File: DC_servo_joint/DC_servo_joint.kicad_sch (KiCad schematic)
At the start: 49 parts, among them U1 AS5600, U2 ESP32-C3-WROOM-02, U3 SP3485EN, U5 TPS563200

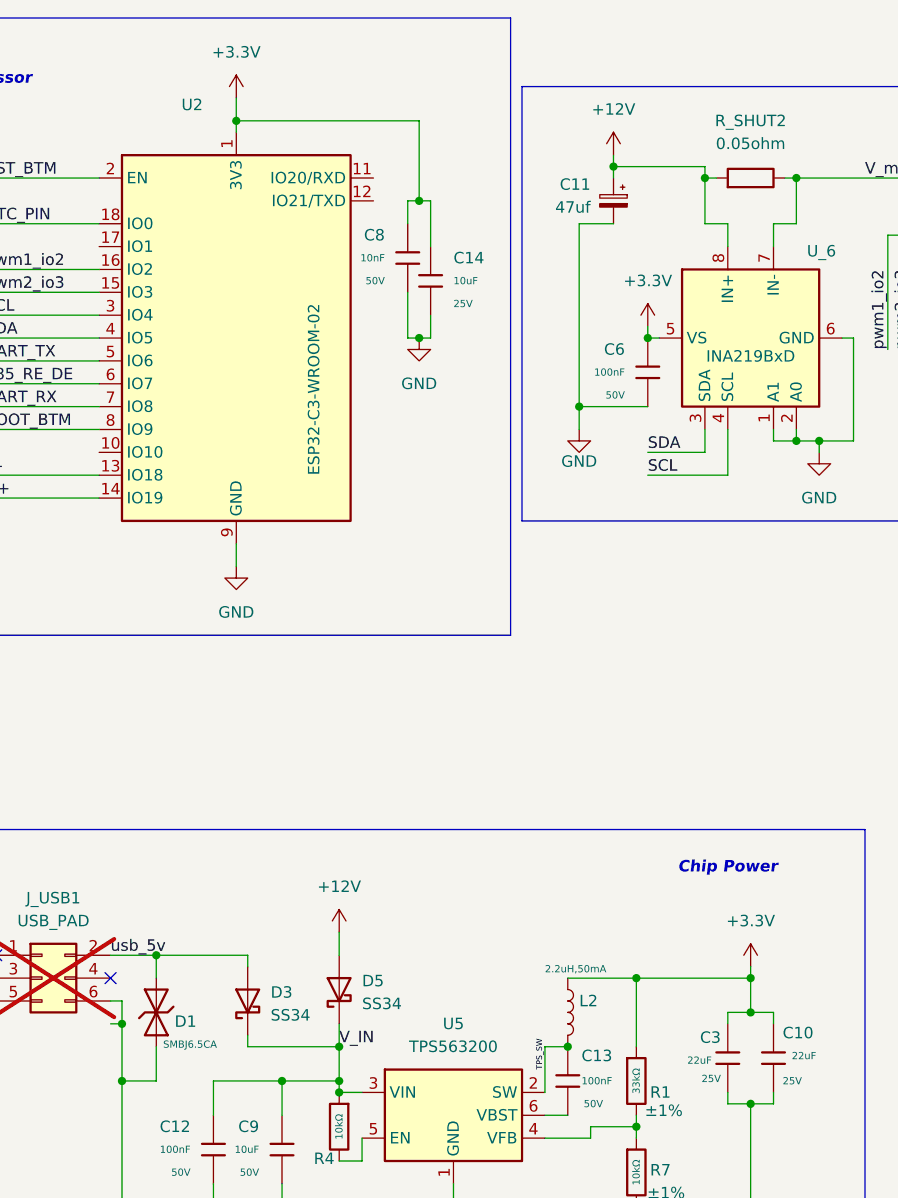
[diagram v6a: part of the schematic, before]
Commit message: Fix the 3.3V power layout
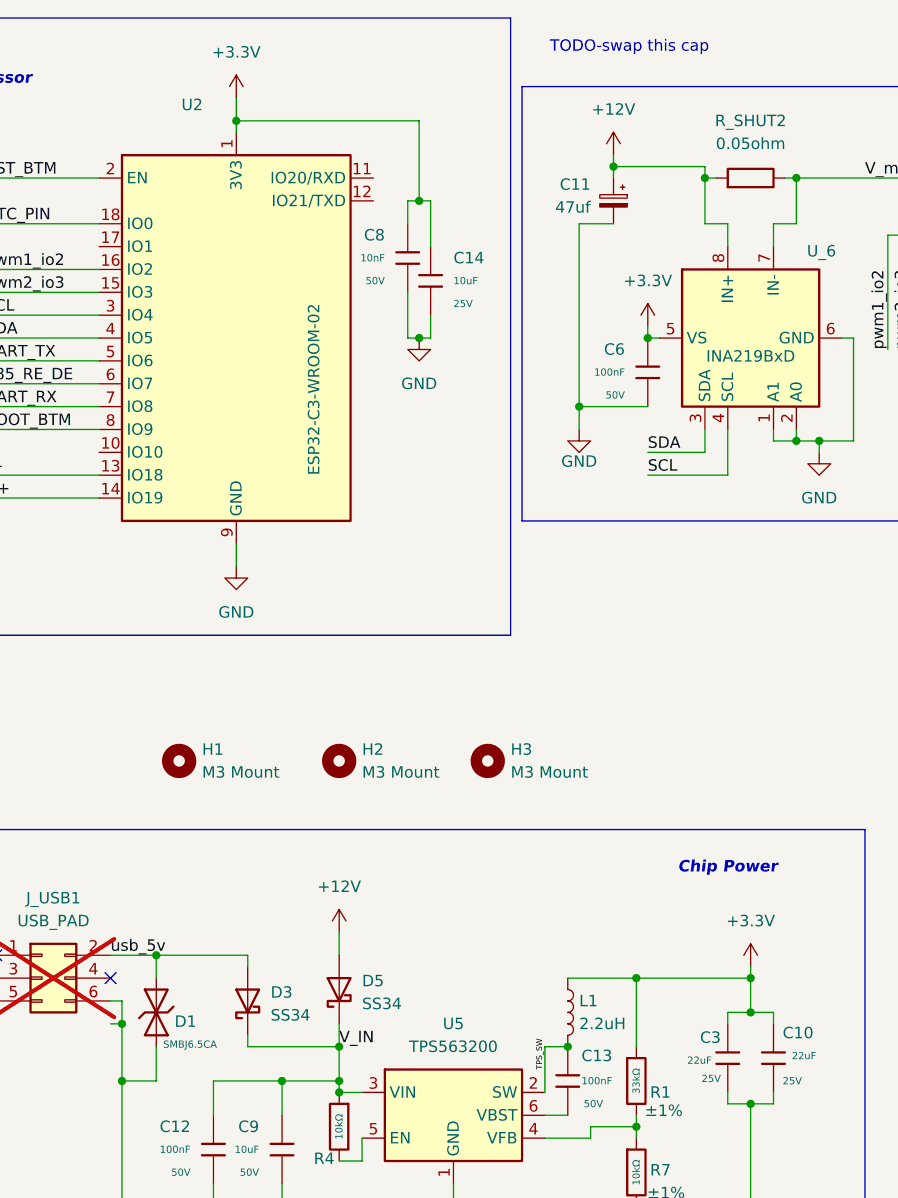
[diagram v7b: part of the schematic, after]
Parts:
- removed L2: 2.2uH,50mA, PCM_JLCPCB:L_0805, symbol PCM_JLCPCB-Inductors:2.2uH,50mA
- added H1, H2, H3: M3 Mount, MountingHole:MountingHole_3.2mm_M3_DIN965, symbol Mechanical:MountingHole
- added L1: 2.2uH, Inductor_SMD:L_Vishay_IHLP-1616, symbol Device:L
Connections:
- net +3.3V: now also L1.1
- net TPS_SW: now also L1.2
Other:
- note added: "TODO-swap this cap"

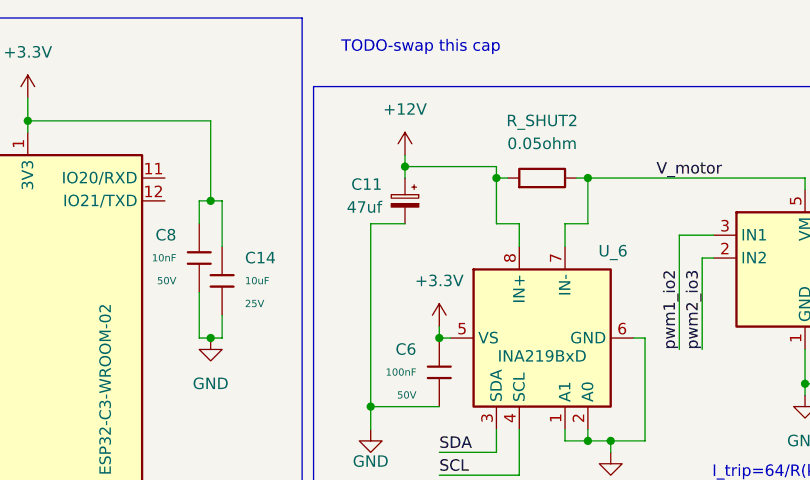
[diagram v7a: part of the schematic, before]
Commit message: Update Big cap selection. Better layout of power trace. Update silk screen. Fix lots of DRC vialation.
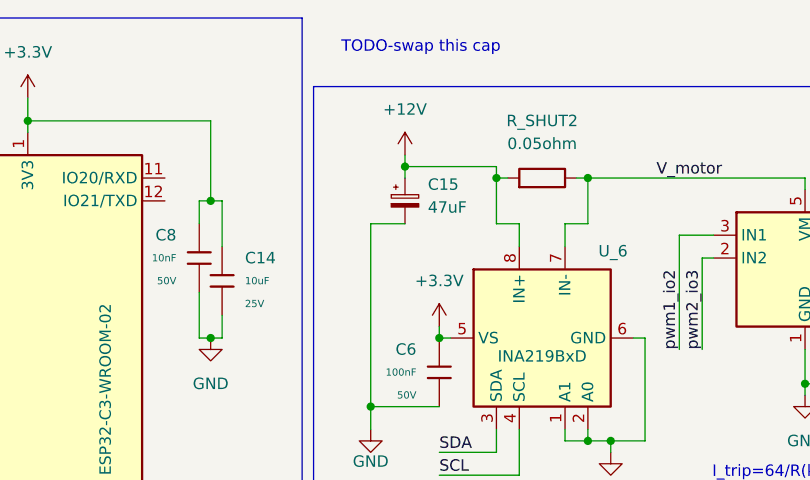
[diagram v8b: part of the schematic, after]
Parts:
- removed C11: 47uf, Capacitor_SMD:CP_Elec_6.3x5.4, symbol Device:C_Polarized_Small
- added C15: 47uF, Capacitor_THT:CP_Radial_D8.0mm_P3.50mm, symbol Device:C_Polarized_Small
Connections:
- net +12V: now also C15.1
- net GND: now also C15.2
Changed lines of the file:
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@@
+	)
+	(symbol
+		(lib_id "Device:C_Polarized_Small")
+		(at 184.15 39.37 0)
+		(unit 1)
+		(exclude_from_sim no)
+		(in_bom yes)
+		(on_board yes)
+		(dnp no)
+		(fields_autoplaced yes)
+		(property "Reference" "C15"
+			(at 186.69 37.5538 0)
+			(effects
+				(font
+					(size 1.27 1.27)
+				)
+				(justify left)
+			)
+		)
+		(property "Value" "47uF"
+			(at 186.69 40.0938 0)
+			(effects
+				(font
+					(size 1.27 1.27)
+				)
+				(justify left)
+			)
+		)
+		(property "Footprint" "Capacitor_THT:CP_Radial_D8.0mm_P3.50mm"
+			(at 184.15 39.37 0)
+			(effects
+				(font
+					(size 1.27 1.27)
+				)
+				(hide yes)
+			)
+		)
+		(property "Datasheet" "~"
+			(at 184.15 39.37 0)
+			(effects
+				(font
+					(size 1.27 1.27)
+				)
+				(hide yes)
+			)
+		)
+		(property "Description" "Polarized capacitor, small symbol"
+			(at 184.15 39.37 0)
+			(effects
+				(font
+					(size 1.27 1.27)
+				)
+				(hide yes)
+			)
+		)
+		(pin "1"
+		)
+		(pin "2"
+		)
+		(instances
+			(project ""
+				(path "/c8f8ac5e-0b71-42b6-88d1-0b81b7fe4cbf"
+					(reference "C15")
+					(unit 1)
+				)
+			)
+		)
 	)
 	(symbol
@@
 					(unit 1)
 				)
-			)
-		)
-	)
-	(symbol
-		(lib_id "Device:C_Polarized_Small")
-		(at 184.15 39.37 0)
-		(mirror y)
-		(unit 1)
-		(exclude_from_sim no)
-		(in_bom yes)
-		(on_board yes)
-		(dnp no)
-		(fields_autoplaced yes)
-		(property "Reference" "C11"
-			(at 181.61 37.5538 0)
-			(effects
-				(font
-					(size 1.27 1.27)
-				)
-				(justify left)
-			)
-		)
-		(property "Value" "47uf"
-			(at 181.61 40.0938 0)
-			(effects
-				(font
-					(size 1.27 1.27)
-				)
-				(justify left)
-			)
-		)
-		(property "Footprint" "Capacitor_SMD:CP_Elec_6.3x5.4"
-			(at 184.15 39.37 0)
-			(effects
-				(font
-					(size 1.27 1.27)
-				)
-				(hide yes)
-			)
-		)
-		(property "Datasheet" "~"
-			(at 184.15 39.37 0)
-			(effects
-				(font
-					(size 1.27 1.27)
-				)
-				(hide yes)
-			)
-		)
-		(property "Description" "Polarized capacitor, small symbol"
-			(at 184.15 39.37 0)
-			(effects
-				(font
-					(size 1.27 1.27)
-				)
-				(hide yes)
-			)
-		)
-		(pin "1"
-		)
-		(pin "2"
-		)
-		(instances
-			(project ""
-				(path "/c8f8ac5e-0b71-42b6-88d1-0b81b7fe4cbf"
-					(reference "C11")
-					(unit 1)
-				)
